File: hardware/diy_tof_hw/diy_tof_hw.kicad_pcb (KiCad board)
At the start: 2 copper layers, 100 x 80 mm, 1 part, among them U1 NUCLEO-F042K6

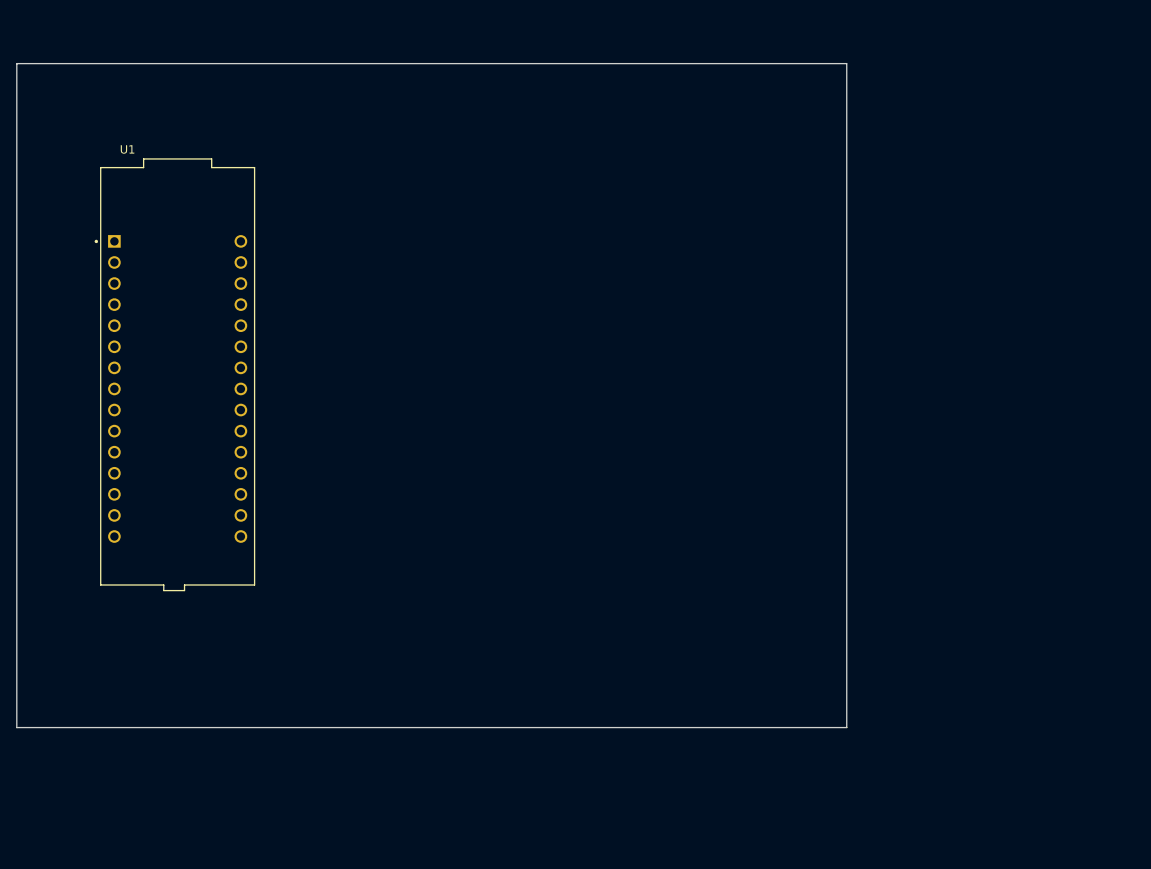
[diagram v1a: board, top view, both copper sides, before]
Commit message: [hardware] added schematics and library components for the laser driver as well as TIA circuit
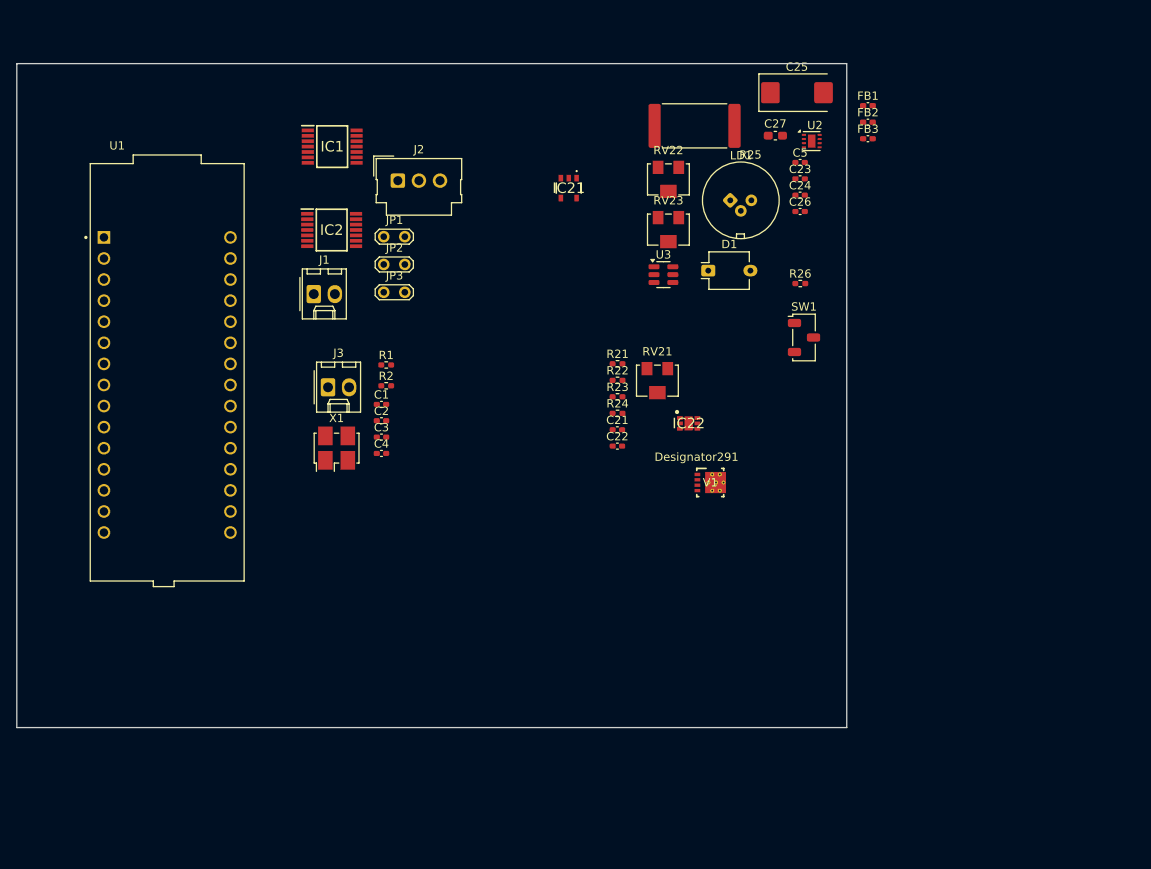
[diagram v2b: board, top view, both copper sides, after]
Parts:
- added C1: 100n, Capacitor_SMD:C_0402_1005Metric_Pad0.74x0.62mm_HandSolder, F.Cu at (83.4, 76.1)
- added C2: 1u, Capacitor_SMD:C_0402_1005Metric_Pad0.74x0.62mm_HandSolder, F.Cu at (83.4, 78.0)
- added C21: 1p, Capacitor_SMD:C_0402_1005Metric_Pad0.74x0.62mm_HandSolder, F.Cu at (111.9, 79.1)
- added C22: 100n, Capacitor_SMD:C_0402_1005Metric_Pad0.74x0.62mm_HandSolder, F.Cu at (111.9, 81.1)
- added C23: 100n, Capacitor_SMD:C_0402_1005Metric_Pad0.74x0.62mm_HandSolder, F.Cu at (133.9, 48.9)
- added C24: 100n, Capacitor_SMD:C_0402_1005Metric_Pad0.74x0.62mm_HandSolder, F.Cu at (133.9, 50.9)
- added C25: 6.8u, Capacitor_Tantalum_SMD:CP_EIA-7343-43_Kemet-X_Pad2.25x2.55mm_HandSolder, F.Cu at (133.5, 38.5)
- added C26: 100n, Capacitor_SMD:C_0402_1005Metric_Pad0.74x0.62mm_HandSolder, F.Cu at (133.9, 52.8)
- added C27: 2.2u, Capacitor_SMD:C_0603_1608Metric_Pad1.08x0.95mm_HandSolder, F.Cu at (130.9, 43.7)
- added C3: 1u, Capacitor_SMD:C_0402_1005Metric_Pad0.74x0.62mm_HandSolder, F.Cu at (83.4, 80.0)
- added C4: 100n, Capacitor_SMD:C_0402_1005Metric_Pad0.74x0.62mm_HandSolder, F.Cu at (83.4, 82.0)
- added C5: 1p, Capacitor_SMD:C_0402_1005Metric_Pad0.74x0.62mm_HandSolder, F.Cu at (133.9, 46.9)
- added D1: BPW34, OptoDevice:Osram_DIL2_4.3x4.65mm_P5.08mm, F.Cu at (122.8, 59.9)
- added FB1: FerriteBead, Inductor_SMD:L_0402_1005Metric_Pad0.77x0.64mm_HandSolder, F.Cu at (142.1, 40.1)
- added FB2: FerriteBead, Inductor_SMD:L_0402_1005Metric_Pad0.77x0.64mm_HandSolder, F.Cu at (142.1, 42.1)
- added FB3: FerriteBead, Inductor_SMD:L_0402_1005Metric_Pad0.77x0.64mm_HandSolder, F.Cu at (142.1, 44.0)
- added IC1: TDC7200PWR, TDC7200:SOP65P640X120-14N, F.Cu at (77.5, 45.0)
- added IC2: TDC7200PWR, TDC7200:SOP65P640X120-14N, F.Cu at (77.4, 55.0)
- added IC21: 74LVC1G08QW5-7, 74LVC1G08QW5-7:74LVC1G08QW57, F.Cu at (106.0, 50.0)
- added IC22: LMG1025QDEETQ1, LMG1025:SON65P200X200X80-7N, F.Cu at (120.5, 78.3)
- added J1: Conn_01x02_Pin, Connector_Molex:Molex_KK-254_AE-6410-02A_1x02_P2.54mm_Vertical, F.Cu at (75.3, 62.8)
- added J2: Conn_01x03_Pin, Connector_Molex:Molex_SL_171971-0003_1x03_P2.54mm_Vertical, F.Cu at (85.4, 49.1)
- added J3: Conn_01x02_Pin, Connector_Molex:Molex_KK-254_AE-6410-02A_1x02_P2.54mm_Vertical, F.Cu at (77.0, 74.0)
- added JP1: Jumper_2_Open, TestPoint:TestPoint_2Pads_Pitch2.54mm_Drill0.8mm, F.Cu at (83.7, 55.9)
- added JP2: Jumper_2_Open, TestPoint:TestPoint_2Pads_Pitch2.54mm_Drill0.8mm, F.Cu at (83.7, 59.2)
- added JP3: 12Vin select, TestPoint:TestPoint_2Pads_Pitch2.54mm_Drill0.8mm, F.Cu at (83.7, 62.5)
- added LD1: D_Laser_Photo_MType, OptoDevice:LaserDiode_TO5-D9-3, F.Cu at (125.5, 51.5)
- added R1: 20k, Resistor_SMD:R_0402_1005Metric_Pad0.72x0.64mm_HandSolder, F.Cu at (84.0, 71.3)
- added R2: 39k, Resistor_SMD:R_0402_1005Metric_Pad0.72x0.64mm_HandSolder, F.Cu at (84.0, 73.8)
- added R21: 510, Resistor_SMD:R_0402_1005Metric_Pad0.72x0.64mm_HandSolder, F.Cu at (111.9, 71.2)
- added R22: 0, Resistor_SMD:R_0402_1005Metric_Pad0.72x0.64mm_HandSolder, F.Cu at (111.9, 73.2)
- added R23: 2, Resistor_SMD:R_0402_1005Metric_Pad0.72x0.64mm_HandSolder, F.Cu at (111.9, 75.2)
- added R24: 2, Resistor_SMD:R_0402_1005Metric_Pad0.72x0.64mm_HandSolder, F.Cu at (111.9, 77.1)
- added R25: XXX, Resistor_SMD:R_4020_10251Metric, F.Cu at (121.2, 42.5)
- added R26: 51k, Resistor_SMD:R_0402_1005Metric_Pad0.72x0.64mm_HandSolder, F.Cu at (133.9, 61.5)
- added RV21: 100k, Potentiometer_SMD:Potentiometer_Bourns_3224W_Vertical, F.Cu at (116.7, 73.2)
- added RV22: 1k, Potentiometer_SMD:Potentiometer_Bourns_3224W_Vertical, F.Cu at (118.0, 49.0)
- added RV23: 1k, Potentiometer_SMD:Potentiometer_Bourns_3224W_Vertical, F.Cu at (118.0, 55.0)
- added SW1: SW_Nidec_CAS-120A1, Button_Switch_SMD:Nidec_Copal_CAS-120A, F.Cu at (134.3, 68.0)
- added U2: OPA858xDSG, Package_SON:WSON-8-1EP_2x2mm_P0.5mm_EP0.9x1.6mm, F.Cu at (135.3, 44.3)
- added U3: TLV3501AIDBV, Package_TO_SOT_SMD:SOT-23-6, F.Cu at (117.4, 60.4)
- added V1: CSD17578Q3A, CSD17578Q3A:DNH0008A, F.Cu at (123.0, 85.5)
- added X1: SG-5032CAN, Oscillator:Oscillator_SMD_SeikoEpson_SG8002LB-4Pin_5.0x3.2mm_HandSoldering, F.Cu at (78.0, 81.3)
- moved U1 1.35 mm to (57.6, 72.2)
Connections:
- U1 pad CN3_1: unconnected-(U1-PA9/D1-PadCN3_1) -> /Power_Nucleo/int_ele
- U1 pad CN3_12: unconnected-(U1-PA8/D9-PadCN3_12) -> /Power_Nucleo/start_ele
- U1 pad CN3_13: unconnected-(U1-PA11/D10-PadCN3_13) -> /Power_Nucleo/stop_ele
- U1 pad CN3_14: unconnected-(U1-PB5/D11-PadCN3_14) -> /Power_Nucleo/spi_mosi
- U1 pad CN3_15: unconnected-(U1-PB4/D12-PadCN3_15) -> /Power_Nucleo/spi_miso
- U1 pad CN3_2: unconnected-(U1-PA10/D0-PadCN3_2) -> /Power_Nucleo/int_opt
- U1 pad CN3_4: unconnected-(U1-GND_CN3-PadCN3_4) -> GND
- U1 pad CN3_6: unconnected-(U1-PB0/D3-PadCN3_6) -> /Power_Nucleo/start_opt
- U1 pad CN3_7: unconnected-(U1-PB7/D4-PadCN3_7) -> /Power_Nucleo/spi_cs_opt
- U1 pad CN3_8: unconnected-(U1-PB6/D5-PadCN3_8) -> /Power_Nucleo/spi_cs_ele
- U1 pad CN3_9: unconnected-(U1-PB1/D6-PadCN3_9) -> /Optoelectronics/LD_Pulse
- U1 pad CN4_1: unconnected-(U1-VIN-PadCN4_1) -> /Power_Nucleo/12_nuc
- U1 pad CN4_10: unconnected-(U1-PA3/A2-PadCN4_10) -> /Power_Nucleo/TDC_enable
- U1 pad CN4_14: unconnected-(U1-+3V3-PadCN4_14) -> 3V3
- U1 pad CN4_15: unconnected-(U1-PB3/D13-PadCN4_15) -> /Power_Nucleo/spi_clk
- U1 pad CN4_2: unconnected-(U1-GND_CN4-PadCN4_2) -> GND
- U1 pad CN4_4: unconnected-(U1-+5V-PadCN4_4) -> +5V_nuc
- U1 pad CN4_9: unconnected-(U1-PA4/A3-PadCN4_9) -> /Power_Nucleo/~{LD_enable}

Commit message: [hardware] added some missing footprints. Generated a footprint for the qioptiq mount
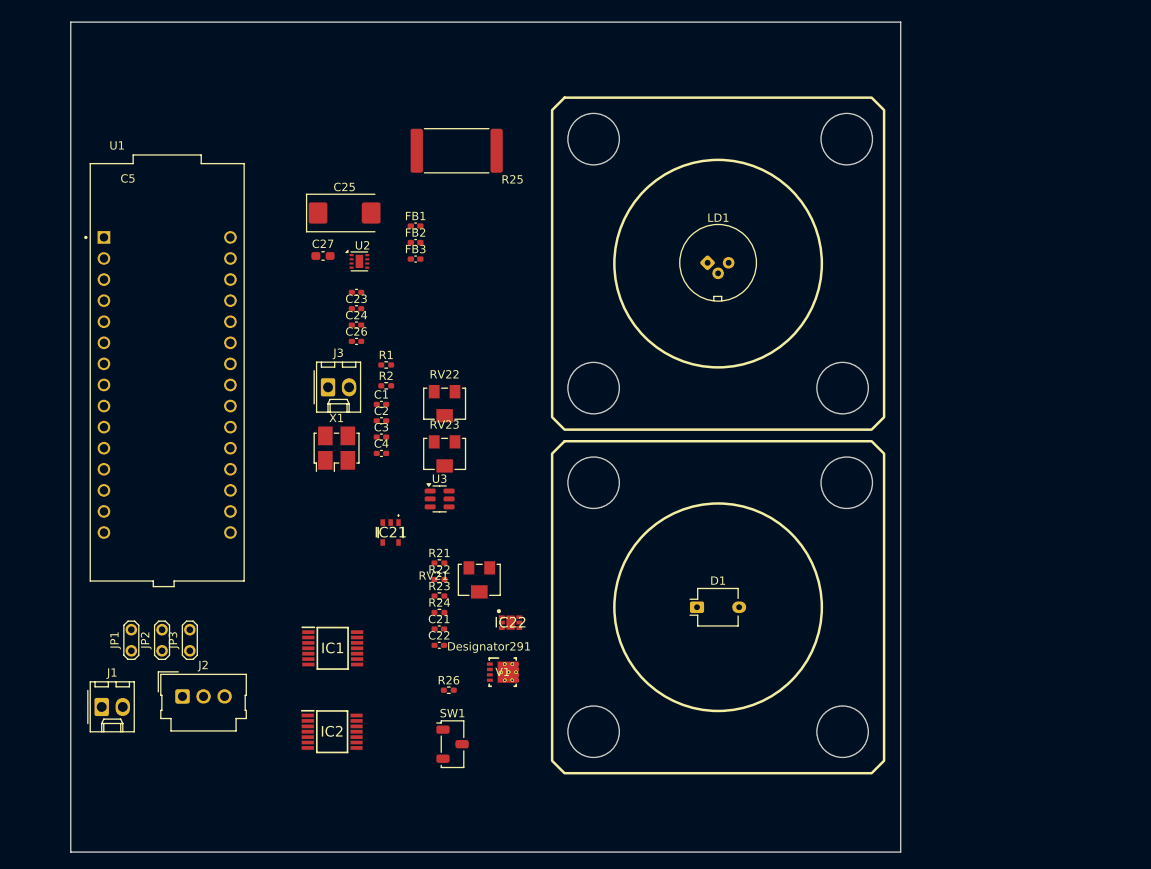
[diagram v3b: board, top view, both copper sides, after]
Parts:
- added X2: ~, user:Qioptiq_Mount, F.Cu at (124.0, 59.1)
- added X3: ~, user:Qioptiq_Mount, F.Cu at (124.0, 100.5)
- moved J2 67.4 mm to (59.5, 111.2)
- moved R26 64.8 mm to (91.6, 110.5)
- moved SW1 64.8 mm to (92.0, 117.0)
- moved IC1 60.5 mm to (77.6, 105.5)
- moved IC2 60.5 mm to (77.5, 115.5)
- moved JP1 58.4 mm to (53.3, 105.8), turned to 90 degrees
- moved FB1 56.4 mm to (87.6, 54.6)
- moved FB2 56.4 mm to (87.6, 56.6)
- moved FB3 56.4 mm to (87.6, 58.5)
- moved C25 56.4 mm to (79.0, 53.0)
- moved C27 56.4 mm to (76.4, 58.2)
- moved U2 56.4 mm to (80.8, 58.8)
- moved J1 55.9 mm to (49.7, 112.5)
- moved C23 55.7 mm to (80.4, 64.5)
- moved C24 55.7 mm to (80.4, 66.5)
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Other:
- board size 100 x 80 mm -> 100 x 100 mm

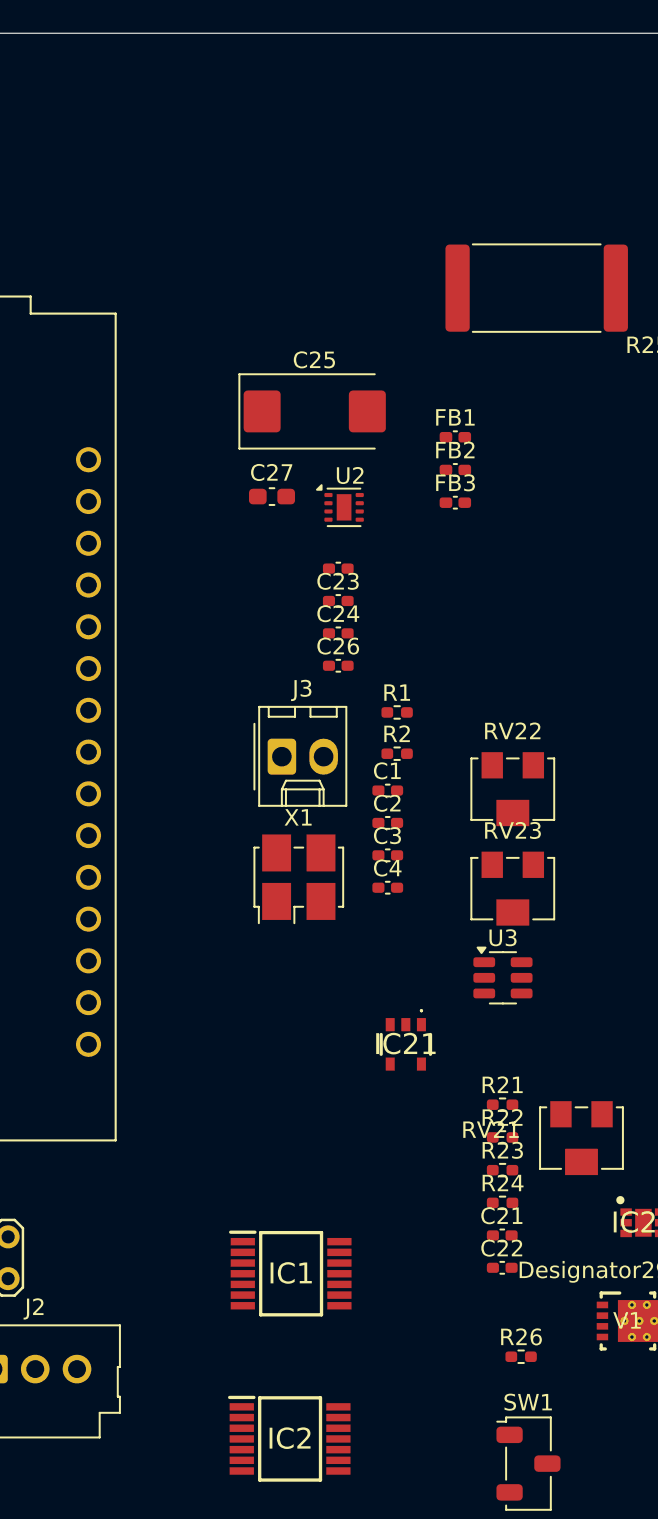
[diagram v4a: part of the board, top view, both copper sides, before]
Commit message: [hardware, firmware] various review findings  - added new signals TDC_opt/ele_enable  - fixed placement and appearance of the optics mount  - added switch for stop signal of the electrical TDC  - replaced "ground bead" with a 0R (in order to have a single clamping point for GND)  - added some additional decoupling caps for the laser driver  - reversed polarisation of the PD  - added a small resistor in between TIA and comparator  - adjusted RC to have higher capacitance and lower resistance  - cleaned up some labels / port names
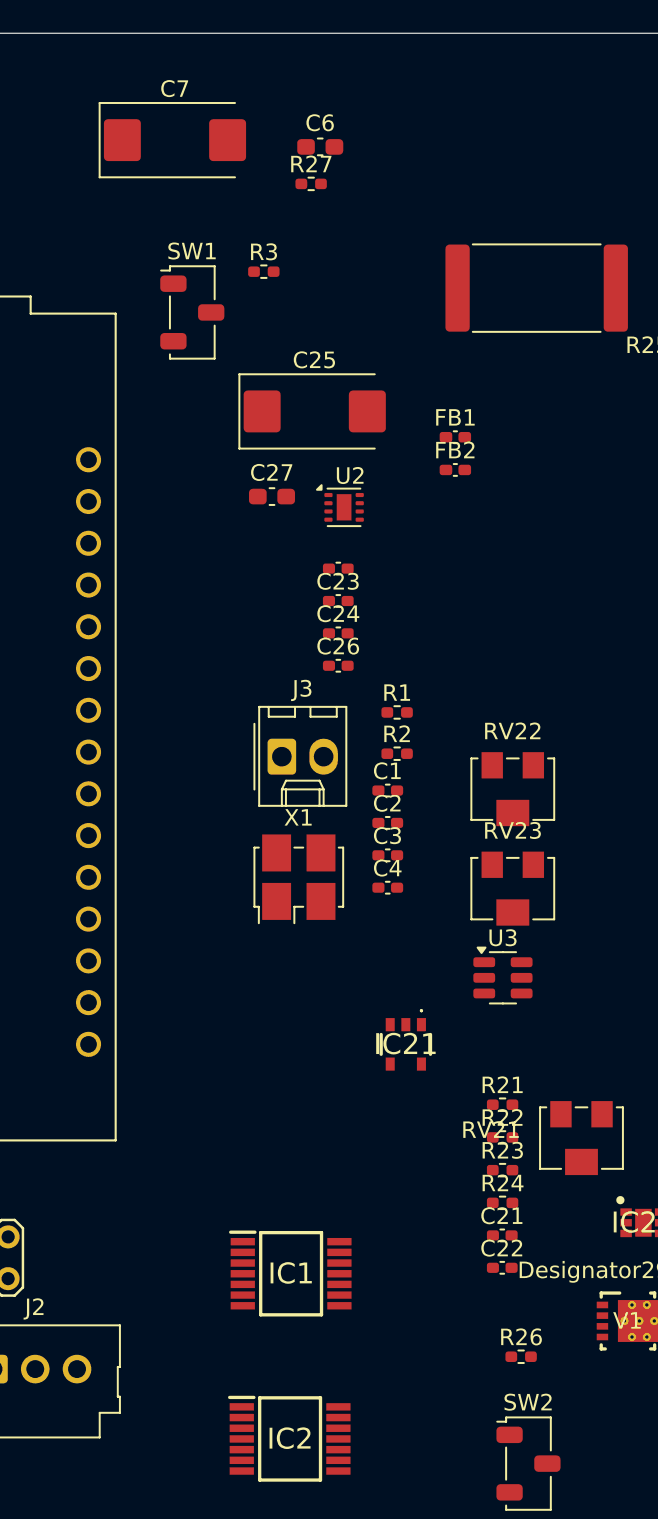
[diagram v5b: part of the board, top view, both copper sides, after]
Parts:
- removed FB3: FerriteBead, Inductor_SMD:L_0402_1005Metric_Pad0.77x0.64mm_HandSolder
- added C6: 2.2u, Capacitor_SMD:C_0603_1608Metric_Pad1.08x0.95mm_HandSolder, F.Cu at (79.3, 36.9)
- added C7: 6.8u, Capacitor_Tantalum_SMD:CP_EIA-7343-43_Kemet-X_Pad2.25x2.55mm_HandSolder, F.Cu at (70.5, 36.5)
- added R27: 100, Resistor_SMD:R_0402_1005Metric_Pad0.72x0.64mm_HandSolder, F.Cu at (78.8, 39.2)
- added R3: 0, Resistor_SMD:R_0402_1005Metric_Pad0.72x0.64mm_HandSolder, F.Cu at (75.9, 44.5)
- added SW1: SW_Nidec_CAS-120A1, Button_Switch_SMD:Nidec_Copal_CAS-120A, F.Cu at (71.6, 47.0)
- C21: value 1p -> 10p
- R21: value 510 -> 51
- RV21: value 100k -> 10k
- renumbered SW1 to SW2
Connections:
- net /Optoelectronics/LD_Pulse renamed /Optoelectronics/LD_pulse
- C5 pad 1: Net-(D1-K) -> Net-(D1-A)
- IC1 pad 1: /Power_Nucleo/TDC_enable -> /Power_Nucleo/TDC_ele_enable
- IC2 pad 1: /Power_Nucleo/TDC_enable -> /Power_Nucleo/TDC_opt_enable
- J3 pad 2: /Power_Nucleo/stop_ele -> Net-(J3-Pin_2)
- R26 pad 1: Net-(D1-K) -> Net-(D1-A)
- SW2 pad 2: Net-(D1-A) -> Net-(D1-K)
- U1 pad CN4_10: /Power_Nucleo/TDC_enable -> /Power_Nucleo/TDC_ele_enable
- U1 pad CN4_11: unconnected-(U1-PA1/A1-PadCN4_11) -> /Power_Nucleo/TDC_opt_enable
- U1 pad CN4_9: /Power_Nucleo/~{LD_enable} -> /Optoelectronics/~{LD_enable}
- U2 pad 3: Net-(D1-K) -> Net-(D1-A)
- U2 pad 6: Net-(U3-+) -> Net-(R27-Pad1)
